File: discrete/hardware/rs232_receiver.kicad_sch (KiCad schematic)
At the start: 18 parts, among them Q4 2N5551, Q5 2N5401, Q6 2N5401

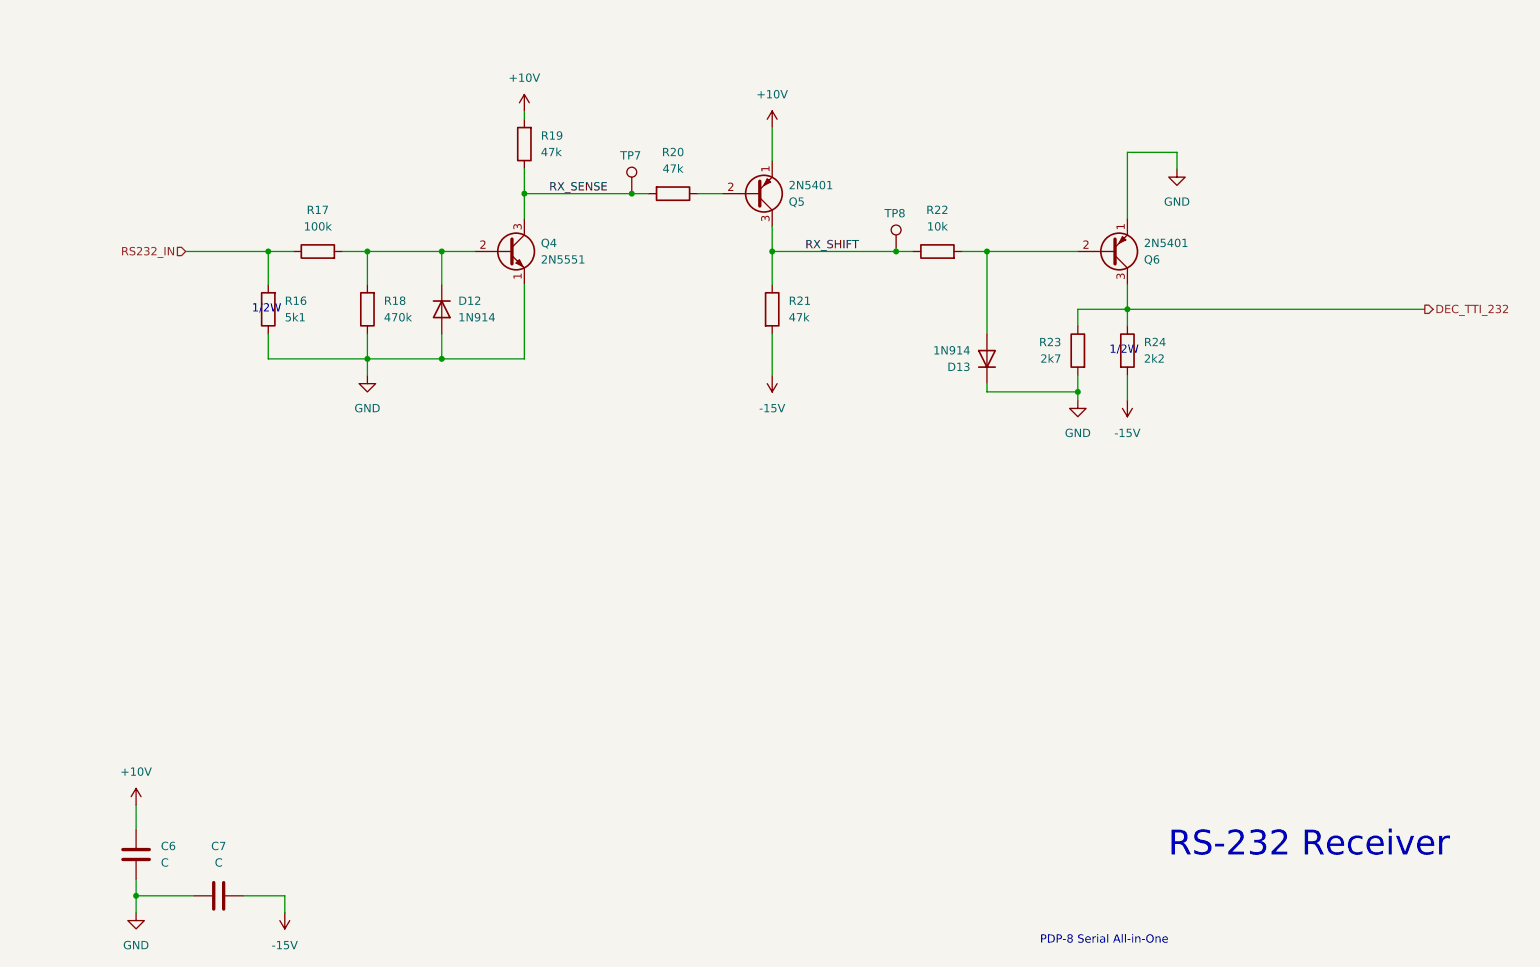
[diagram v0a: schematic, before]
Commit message: Restructured for sheet reuse of rs232 driver. Annotated functional blocks of schematic. Resolved all ERC violations
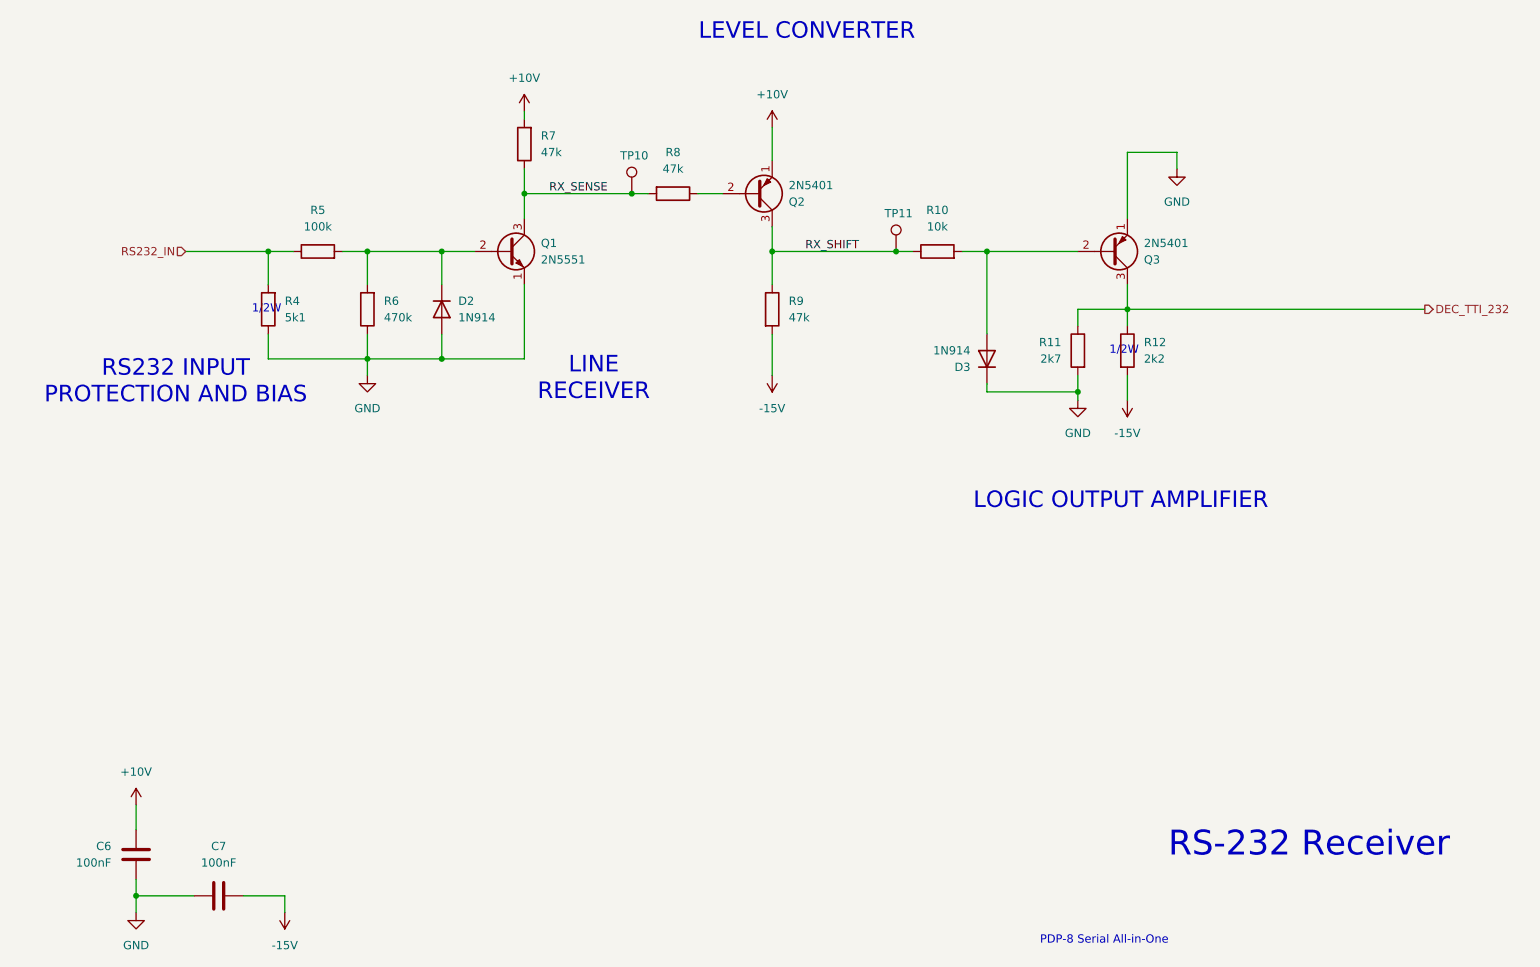
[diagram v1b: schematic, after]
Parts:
- C6, C7: value C -> 100nF
- renumbered D12 to D2, D13 to D3, Q4 to Q1, Q5 to Q2, Q6 to Q3, R22 to R10, R23 to R11, R24 to R12, R16 to R4, R17 to R5, R18 to R6, R19 to R7, R20 to R8, R21 to R9, TP7 to TP10, TP8 to TP11
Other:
- note added: "LEVEL CONVERTER"
- note added: "LINE RECEIVER"
- note added: "LOGIC OUTPUT AMPLIFIER"
- note added: "RS232 INPUT PROTECTION AND BIAS"

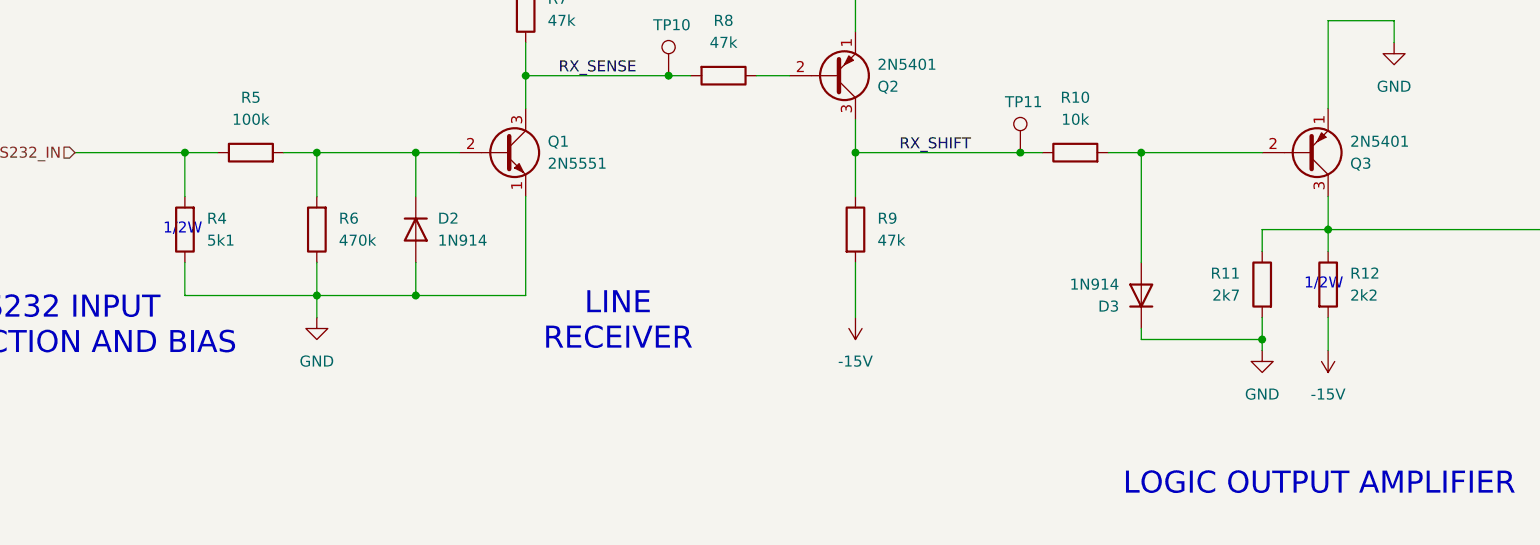
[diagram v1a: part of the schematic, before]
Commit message: Set footprints and component ratings
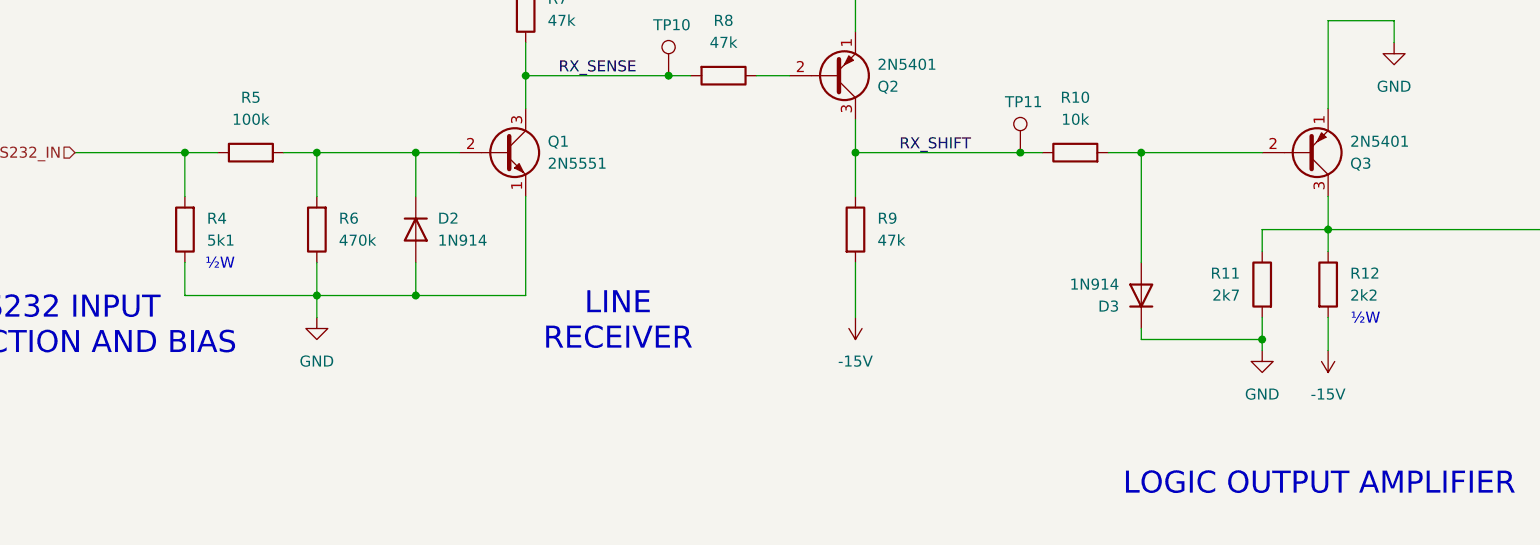
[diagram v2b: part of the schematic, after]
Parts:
- C6, C7: footprint (none) -> Capacitor_THT:C_Disc_D5.0mm_W2.5mm_P2.50mm
- R10, R11, R12, R4, R5, R6, R7, R8, R9: footprint (none) -> Resistor_THT:R_Axial_DIN0207_L6.3mm_D2.5mm_P10.16mm_Horizontal
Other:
- note added: "½W"
- note removed: "1/2W"
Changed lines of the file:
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@@
 	(generator_version "9.0")
 	(paper "A4")
+	(text "½W"
+		(exclude_from_sim no)
+		(at 208.788 103.124 0)
+		(effects
+			(font
+				(size 1.27 1.27)
+			)
+		)
+	)
 	(text "LEVEL CONVERTER"
 		(exclude_from_sim no)
@@
 		)
 	)
-	(text "1/2W"
-		(exclude_from_sim no)
-		(at 72.136 92.71 0)
-		(effects
-			(font
-				(size 1.27 1.27)
-			)
-		)
-	)
 	(text "RS232 INPUT \nPROTECTION AND BIAS"
 		(exclude_from_sim no)
@@
 		)
 	)
+	(text "½W"
+		(exclude_from_sim no)
+		(at 76.454 96.774 0)
+		(effects
+			(font
+				(size 1.27 1.27)
+			)
+		)
+	)
 	(text "LOGIC OUTPUT AMPLIFIER"
 		(exclude_from_sim no)
@@
 			(font
 				(size 2.54 2.54)
-			)
-		)
-	)
-	(text "1/2W"
-		(exclude_from_sim no)
-		(at 203.962 99.06 0)
-		(effects
-			(font
-				(size 1.27 1.27)
 			)
 		)
@@
 			)
 		)
-		(property "Footprint" ""
+		(property "Footprint" "Resistor_THT:R_Axial_DIN0207_L6.3mm_D2.5mm_P10.16mm_Horizontal"
 			(at 113.538 67.31 90)
 			(effects
@@
 			)
 		)
-		(property "Footprint" ""
+		(property "Footprint" "Resistor_THT:R_Axial_DIN0207_L6.3mm_D2.5mm_P10.16mm_Horizontal"
 			(at 175.26 85.598 90)
 			(effects
@@
 		(on_board yes)
 		(dnp no)
-		(fields_autoplaced yes)
 		(property "Reference" "R4"
 			(at 74.93 91.4399 0)
@@
 			)
 		)
-		(property "Footprint" ""
+		(property "Footprint" "Resistor_THT:R_Axial_DIN0207_L6.3mm_D2.5mm_P10.16mm_Horizontal"
 			(at 74.168 92.71 90)
 			(effects
@@
 			)
 		)
-		(property "Footprint" ""
+		(property "Footprint" "Resistor_THT:R_Axial_DIN0207_L6.3mm_D2.5mm_P10.16mm_Horizontal"
 			(at 198.628 99.06 90)
 			(effects
@@
 			)
 		)
-		(property "Footprint" ""
+		(property "Footprint" "Capacitor_THT:C_Disc_D5.0mm_W2.5mm_P2.50mm"
 			(at 51.1048 180.34 0)
 			(effects
@@
 			)
 		)
-		(property "Footprint" ""
+		(property "Footprint" "Resistor_THT:R_Axial_DIN0207_L6.3mm_D2.5mm_P10.16mm_Horizontal"
 			(at 89.408 92.71 90)
 			(effects
@@
 			)
 		)
-		(property "Footprint" ""
+		(property "Footprint" "Resistor_THT:R_Axial_DIN0207_L6.3mm_D2.5mm_P10.16mm_Horizontal"
 			(at 148.082 92.71 90)
 			(effects
@@
 			)
 		)
-		(property "Footprint" ""
+		(property "Footprint" "Resistor_THT:R_Axial_DIN0207_L6.3mm_D2.5mm_P10.16mm_Horizontal"
 			(at 202.692 99.06 90)
 			(effects
@@
 			)
 		)
-		(property "Footprint" ""
+		(property "Footprint" "Capacitor_THT:C_Disc_D5.0mm_W2.5mm_P2.50mm"
 			(at 68.58 181.9148 0)
 			(effects
@@
 			)
 		)
-		(property "Footprint" ""
+		(property "Footprint" "Resistor_THT:R_Axial_DIN0207_L6.3mm_D2.5mm_P10.16mm_Horizontal"
 			(at 134.62 73.152 90)
 			(effects
@@
 			)
 		)
-		(property "Footprint" ""
+		(property "Footprint" "Resistor_THT:R_Axial_DIN0207_L6.3mm_D2.5mm_P10.16mm_Horizontal"
 			(at 80.01 85.598 90)
 			(effects

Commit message: Added holeless flip-chip layout. Footprints assigned.
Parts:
- R10, R11, R5, R6, R7, R8, R9: footprint Resistor_THT:R_Axial_DIN0207_L6.3mm_D2.5mm_P10.16mm_Horizontal -> Resistor_THT:R_Axial_DIN0207_L6.3mm_D2.5mm_P7.62mm_Horizontal
- R12, R4: footprint Resistor_THT:R_Axial_DIN0207_L6.3mm_D2.5mm_P10.16mm_Horizontal -> Resistor_THT:R_Axial_DIN0309_L9.0mm_D3.2mm_P12.70mm_Horizontal
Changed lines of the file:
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@@
 			)
 		)
-		(property "Footprint" "Resistor_THT:R_Axial_DIN0207_L6.3mm_D2.5mm_P10.16mm_Horizontal"
+		(property "Footprint" "Resistor_THT:R_Axial_DIN0207_L6.3mm_D2.5mm_P7.62mm_Horizontal"
 			(at 113.538 67.31 90)
 			(effects
@@
 			)
 		)
-		(property "Footprint" "Resistor_THT:R_Axial_DIN0207_L6.3mm_D2.5mm_P10.16mm_Horizontal"
+		(property "Footprint" "Resistor_THT:R_Axial_DIN0207_L6.3mm_D2.5mm_P7.62mm_Horizontal"
 			(at 175.26 85.598 90)
 			(effects
@@
 			)
 		)
-		(property "Footprint" "Resistor_THT:R_Axial_DIN0207_L6.3mm_D2.5mm_P10.16mm_Horizontal"
+		(property "Footprint" "Resistor_THT:R_Axial_DIN0309_L9.0mm_D3.2mm_P12.70mm_Horizontal"
 			(at 74.168 92.71 90)
 			(effects
@@
 			)
 		)
-		(property "Footprint" "Resistor_THT:R_Axial_DIN0207_L6.3mm_D2.5mm_P10.16mm_Horizontal"
+		(property "Footprint" "Resistor_THT:R_Axial_DIN0207_L6.3mm_D2.5mm_P7.62mm_Horizontal"
 			(at 198.628 99.06 90)
 			(effects
@@
 			)
 		)
-		(property "Footprint" "Resistor_THT:R_Axial_DIN0207_L6.3mm_D2.5mm_P10.16mm_Horizontal"
+		(property "Footprint" "Resistor_THT:R_Axial_DIN0207_L6.3mm_D2.5mm_P7.62mm_Horizontal"
 			(at 89.408 92.71 90)
 			(effects
@@
 			)
 		)
-		(property "Footprint" "Resistor_THT:R_Axial_DIN0207_L6.3mm_D2.5mm_P10.16mm_Horizontal"
+		(property "Footprint" "Resistor_THT:R_Axial_DIN0207_L6.3mm_D2.5mm_P7.62mm_Horizontal"
 			(at 148.082 92.71 90)
 			(effects
@@
 			)
 		)
-		(property "Footprint" "Resistor_THT:R_Axial_DIN0207_L6.3mm_D2.5mm_P10.16mm_Horizontal"
+		(property "Footprint" "Resistor_THT:R_Axial_DIN0309_L9.0mm_D3.2mm_P12.70mm_Horizontal"
 			(at 202.692 99.06 90)
 			(effects
@@
 			)
 		)
-		(property "Footprint" "Resistor_THT:R_Axial_DIN0207_L6.3mm_D2.5mm_P10.16mm_Horizontal"
+		(property "Footprint" "Resistor_THT:R_Axial_DIN0207_L6.3mm_D2.5mm_P7.62mm_Horizontal"
 			(at 134.62 73.152 90)
 			(effects
@@
 			)
 		)
-		(property "Footprint" "Resistor_THT:R_Axial_DIN0207_L6.3mm_D2.5mm_P10.16mm_Horizontal"
+		(property "Footprint" "Resistor_THT:R_Axial_DIN0207_L6.3mm_D2.5mm_P7.62mm_Horizontal"
 			(at 80.01 85.598 90)
 			(effects

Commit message: New footprints and symbols. PCB layout begun
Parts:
- removed TP10, TP11: TestPoint, TestPoint:TestPoint_Loop_D3.50mm_Drill0.9mm_Beaded, symbol Connector:TestPoint
- renumbered D2 to D5, D3 to D6, R7 to R10, R8 to R11, R9 to R12, R10 to R13, R11 to R14, R12 to R15, R4 to R7, R5 to R8, R6 to R9

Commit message: Geographic reannotation of PCB
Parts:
- renumbered D5 to D4, R13 to R10, R14 to R11, R15 to R12, R7 to R4, R9 to R5, R8 to R6, R11 to R7, R10 to R8, R12 to R9
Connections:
- net RX_SENSE: now also R7.1; no longer R7.2
- net at Q2.2 (B): now also R7.2; no longer R7.1
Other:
- moved on the sheet: R7
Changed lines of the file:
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@@
 		(dnp no)
 		(fields_autoplaced yes)
-		(property "Reference" "R10"
+		(property "Reference" "R8"
 			(at 114.3 66.0399 0)
 			(effects
@@
 			(project "PDP-8-Serial-Discrete"
 				(path "/b0fbf6eb-12c5-46d4-80aa-25b95de8bd79/45ac807a-2577-4409-8b2a-1bfaf4f033b6"
-					(reference "R10")
+					(reference "R8")
 					(unit 1)
 				)
@@
 		(dnp no)
 		(fields_autoplaced yes)
-		(property "Reference" "R13"
+		(property "Reference" "R10"
 			(at 175.26 77.47 90)
 			(effects
@@
 			(project "PDP-8-Serial-Discrete"
 				(path "/b0fbf6eb-12c5-46d4-80aa-25b95de8bd79/45ac807a-2577-4409-8b2a-1bfaf4f033b6"
-					(reference "R13")
+					(reference "R10")
 					(unit 1)
 				)
@@
 		(on_board yes)
 		(dnp no)
-		(property "Reference" "R7"
+		(property "Reference" "R4"
 			(at 74.93 91.4399 0)
 			(effects
@@
 			(project "PDP-8-Serial-Discrete"
 				(path "/b0fbf6eb-12c5-46d4-80aa-25b95de8bd79/45ac807a-2577-4409-8b2a-1bfaf4f033b6"
-					(reference "R7")
+					(reference "R4")
 					(unit 1)
 				)
@@
 		(on_board yes)
 		(dnp no)
-		(property "Reference" "R14"
+		(property "Reference" "R11"
 			(at 194.31 97.7899 0)
 			(effects
@@
 			(project "PDP-8-Serial-Discrete"
 				(path "/b0fbf6eb-12c5-46d4-80aa-25b95de8bd79/45ac807a-2577-4409-8b2a-1bfaf4f033b6"
-					(reference "R14")
+					(reference "R11")
 					(unit 1)
 				)
@@
 		(dnp no)
 		(fields_autoplaced yes)
-		(property "Reference" "R9"
+		(property "Reference" "R5"
 			(at 90.17 91.4399 0)
 			(effects
@@
 			(project "PDP-8-Serial-Discrete"
 				(path "/b0fbf6eb-12c5-46d4-80aa-25b95de8bd79/45ac807a-2577-4409-8b2a-1bfaf4f033b6"
-					(reference "R9")
+					(reference "R5")
 					(unit 1)
 				)
@@
 		(dnp no)
 		(fields_autoplaced yes)
-		(property "Reference" "R12"
+		(property "Reference" "R9"
 			(at 152.4 91.4399 0)
 			(effects
@@
 			(project "PDP-8-Serial-Discrete"
 				(path "/b0fbf6eb-12c5-46d4-80aa-25b95de8bd79/45ac807a-2577-4409-8b2a-1bfaf4f033b6"
-					(reference "R12")
+					(reference "R9")
 					(unit 1)
 				)
@@
 		(dnp no)
 		(fields_autoplaced yes)
-		(property "Reference" "R15"
+		(property "Reference" "R12"
 			(at 207.01 97.7899 0)
 			(effects
@@
 			(project "PDP-8-Serial-Discrete"
 				(path "/b0fbf6eb-12c5-46d4-80aa-25b95de8bd79/45ac807a-2577-4409-8b2a-1bfaf4f033b6"
-					(reference "R15")
+					(reference "R12")
 					(unit 1)
 				)
@@
 		(dnp no)
 		(fields_autoplaced yes)
-		(property "Reference" "D5"
+		(property "Reference" "D4"
 			(at 101.6 91.4399 90)
 			(effects
@@
 			(project "PDP-8-Serial-Discrete"
 				(path "/b0fbf6eb-12c5-46d4-80aa-25b95de8bd79/45ac807a-2577-4409-8b2a-1bfaf4f033b6"
-					(reference "D5")
+					(reference "D4")
 					(unit 1)
 				)
@@
 	(symbol
 		(lib_id "Device:R")
-		(at 134.62 74.93 270)
-		(unit 1)
-		(exclude_from_sim no)
-		(in_bom yes)
-		(on_board yes)
-		(dnp no)
-		(fields_autoplaced yes)
-		(property "Reference" "R11"
+		(at 134.62 74.93 90)
+		(mirror x)
+		(unit 1)
+		(exclude_from_sim no)
+		(in_bom yes)
+		(on_board yes)
+		(dnp no)
+		(property "Reference" "R7"
 			(at 134.62 68.58 90)
 			(effects
@@
 			(project "PDP-8-Serial-Discrete"
 				(path "/b0fbf6eb-12c5-46d4-80aa-25b95de8bd79/45ac807a-2577-4409-8b2a-1bfaf4f033b6"
-					(reference "R11")
+					(reference "R7")
 					(unit 1)
 				)
@@
 		(dnp no)
 		(fields_autoplaced yes)
-		(property "Reference" "R8"
+		(property "Reference" "R6"
 			(at 80.01 77.47 90)
 			(effects
@@
 			(project "PDP-8-Serial-Discrete"
 				(path "/b0fbf6eb-12c5-46d4-80aa-25b95de8bd79/45ac807a-2577-4409-8b2a-1bfaf4f033b6"
-					(reference "R8")
-					(unit 1)
-				)
+					(reference "R6")
+					(unit 1)
+				)

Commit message: Added BOM details
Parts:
- C6, C7: DigiKey_PN (none) -> 490-9145-1-ND; MPN (none) -> RDER71H104K0S1H03A; Manufacturer (none) -> Murata Electronics
- D4, D6: DigiKey_PN (none) -> 1N914B-ND; MPN (none) -> 1N914B; Manufacturer (none) -> onsemi
- Q1: DigiKey_PN (none) -> 4878-2N5551CT-ND; MPN (none) -> 2N5551; Manufacturer (none) -> Diotec Semiconductor
- Q2, Q3: DigiKey_PN (none) -> 4878-2N5401CT-ND; MPN (none) -> 2N5401; Manufacturer (none) -> Diotec Semiconductor
- R10: DigiKey_PN (none) -> 10.0KXBK-ND; MPN (none) -> MFR-25FBF52-10K; Manufacturer (none) -> YAGEO
- R11: DigiKey_PN (none) -> MFR-25FBF52-2K7-ND; MPN (none) -> RES 2.7K OHM 1% 1/4W AXIAL; Manufacturer (none) -> YAGEO
- R12: DigiKey_PN (none) -> MFR-50FRF52-2K2-ND; MPN (none) -> RES 2.2K OHM 1% 1/2W AXIAL; Manufacturer (none) -> YAGEO
- R4: DigiKey_PN (none) -> MFR-50FRF52-5K1-ND; MPN (none) -> MFR-50FRF52-5K1; Manufacturer (none) -> YAGEO
- R5: DigiKey_PN (none) -> MFR-25FBF52-470K-ND; MPN (none) -> MFR-25FBF52-470K; Manufacturer (none) -> YAGEO
- R6: DigiKey_PN (none) -> 100KXBK-ND; MPN (none) -> MFR-25FBF52-100K; Manufacturer (none) -> YAGEO
- R7, R8, R9: DigiKey_PN (none) -> MFR-25FBF52-47K-ND; MPN (none) -> RES 47K OHM 1% 1/4W AXIAL; Manufacturer (none) -> YAGEO
